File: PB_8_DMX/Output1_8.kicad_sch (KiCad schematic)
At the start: 20 parts, among them IC1 AM26C31, IC2 AM26C31, J1 String1, J2 String2, J3 String3, J4 String4, J5 String5, J6 String6, J7 String7, J8 String8

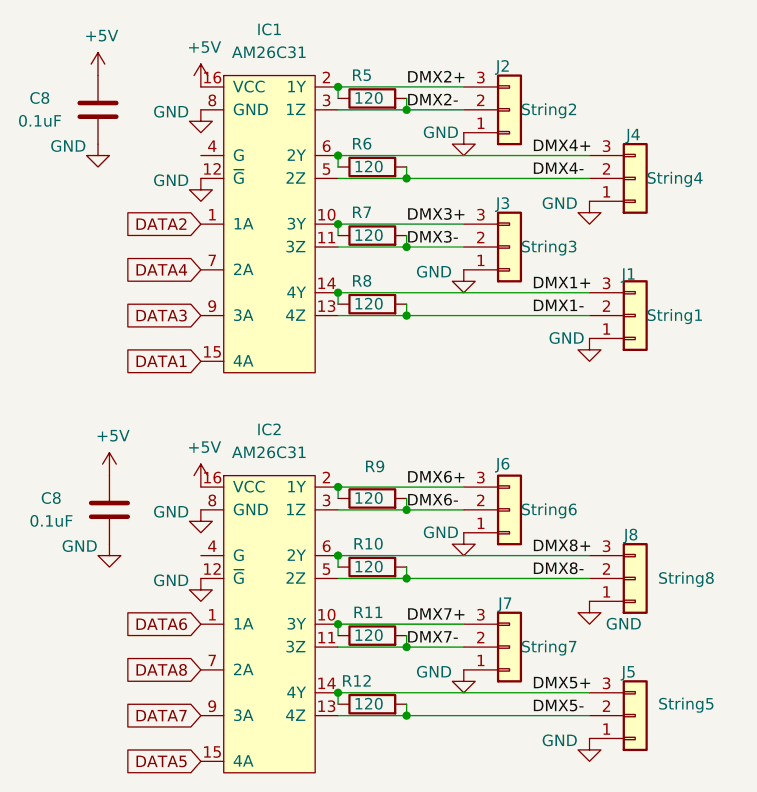
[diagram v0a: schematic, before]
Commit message: remove OLED switch
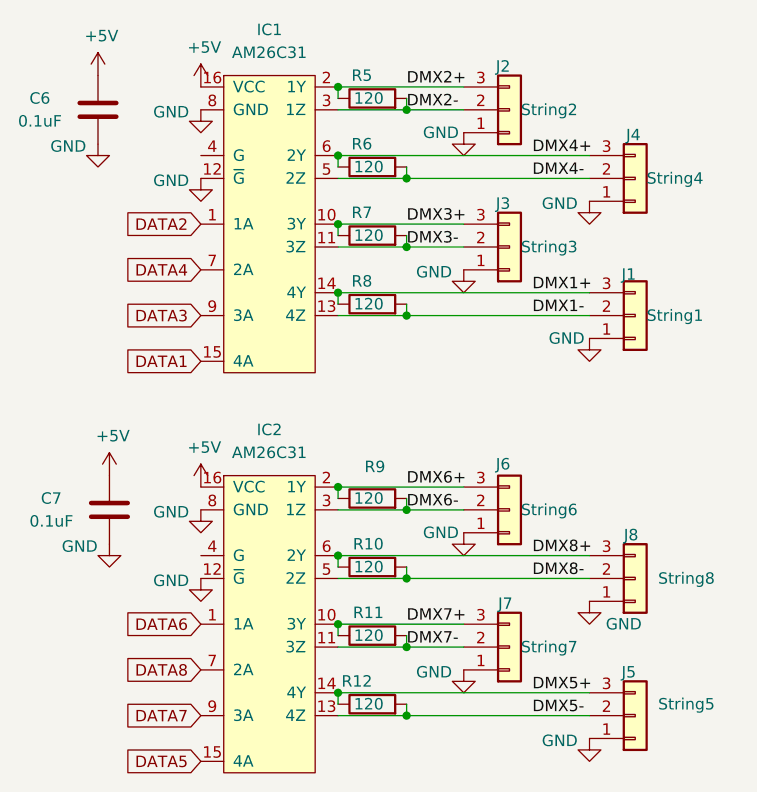
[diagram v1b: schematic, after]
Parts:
- renumbered C8 to C6, C8 to C7
